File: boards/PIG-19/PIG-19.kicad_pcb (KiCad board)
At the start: 4 copper layers, 70.1 x 45.4 mm, 47 parts, among them J1 XT30PW-F, J11 USB4105-GF-A, J2 XT30PW-F, J5 Conn_01x02_Pin, J6 Conn_01x02_Pin, J9 XT30PW-M, Q1 PMOS, SW3 SW_Nidec_CAS-120A1, U1 LM2940S-5.0

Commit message: order this one
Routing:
- net GND: vias 107 -> 104

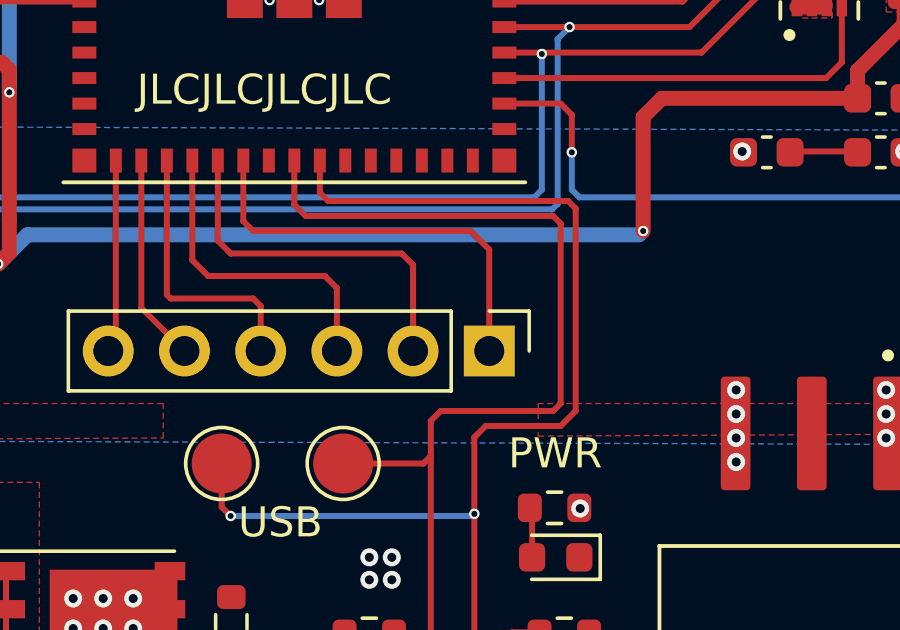
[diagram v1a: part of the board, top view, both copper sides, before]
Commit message: Added BOM for main board
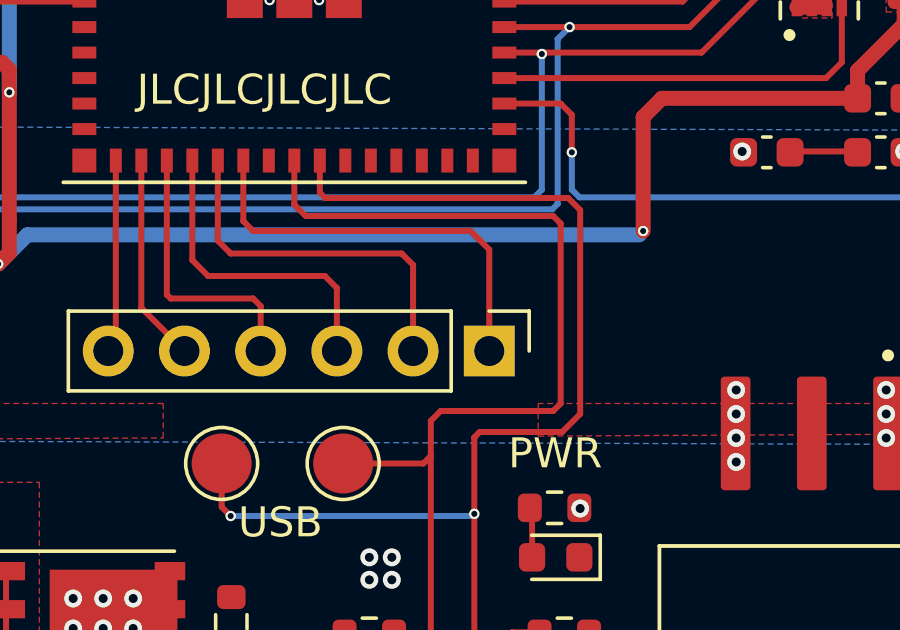
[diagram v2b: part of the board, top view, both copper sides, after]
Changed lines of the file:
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@@
-	)
-	(segment
-		(start 169.25 76.75)
-		(end 169 76.5)
-		(width 0.2)
-		(layer "F.Cu")
-		(net 28)
 	)
 	(segment
@@
 	)
 	(segment
-		(start 169 76.5)
-		(end 161 76.5)
-		(width 0.2)
-		(layer "F.Cu")
-		(net 28)
-	)
-	(segment
-		(start 166.25 84)
-		(end 168.75 84)
-		(width 0.2)
-		(layer "F.Cu")
-		(net 28)
-	)
-	(segment
-		(start 168.75 84)
-		(end 169.25 83.5)
+		(start 165.871955 86.928045)
+		(end 165.871955 84.378045)
 		(width 0.2)
 		(layer "F.Cu")
@@
 	)
 	(segment
-		(start 161 76.5)
-		(end 160.721955 76.221955)
+		(start 164.871955 93.322518)
+		(end 164.871955 94.147518)
 		(width 0.2)
 		(layer "F.Cu")
@@
 	)
 	(segment
-		(start 164.871955 93.322518)
-		(end 164.871955 94.147518)
+		(start 169.4 83.6)
+		(end 169.4 76.8)
 		(width 0.2)
 		(layer "F.Cu")
@@
 	)
 	(segment
-		(start 169.25 83.5)
-		(end 169.25 76.75)
-		(width 0.2)
-		(layer "F.Cu")
-		(net 28)
-	)
-	(segment
-		(start 165.871955 84.378045)
-		(end 166.25 84)
-		(width 0.2)
-		(layer "F.Cu")
-		(net 28)
-	)
-	(segment
-		(start 165.871955 86.928045)
-		(end 165.871955 84.378045)
+		(start 160.9 76.4)
+		(end 160.721955 76.221955)
 		(width 0.2)
 		(layer "F.Cu")
@@
 	)
 	(segment
+		(start 166.05 84.2)
+		(end 168.8 84.2)
+		(width 0.2)
+		(layer "F.Cu")
+		(net 28)
+	)
+	(segment
 		(start 157.75 87)
 		(end 157.45 86.7)
+		(width 0.2)
+		(layer "F.Cu")
+		(net 28)
+	)
+	(segment
+		(start 169 76.4)
+		(end 160.9 76.4)
+		(width 0.2)
+		(layer "F.Cu")
+		(net 28)
+	)
+	(segment
+		(start 169.4 76.8)
+		(end 169 76.4)
 		(width 0.2)
 		(layer "F.Cu")
@@
 	)
 	(segment
+		(start 168.8 84.2)
+		(end 169.4 83.6)
+		(width 0.2)
+		(layer "F.Cu")
+		(net 28)
+	)
+	(segment
 		(start 164.921955 94.197518)
 		(end 165.821955 94.197518)
 		(width 0.2)
 		(layer "F.Cu")
+		(net 28)
+	)
+	(segment
+		(start 165.871955 84.378045)
+		(end 166.05 84.2)
+		(width 0.2)
+		(layer "F.Cu")
